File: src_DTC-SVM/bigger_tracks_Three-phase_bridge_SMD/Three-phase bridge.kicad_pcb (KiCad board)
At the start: 2 copper layers, 377.2 x 318 mm, 105 parts, among them M1 MCP6022-I/P, M2 MCP6022-I/P, P1 CONN_1, P2 POWER_FUSE, P3 CONN_2, P4 CONN_1, P5 CONN_1, P6 POWER_FUSE

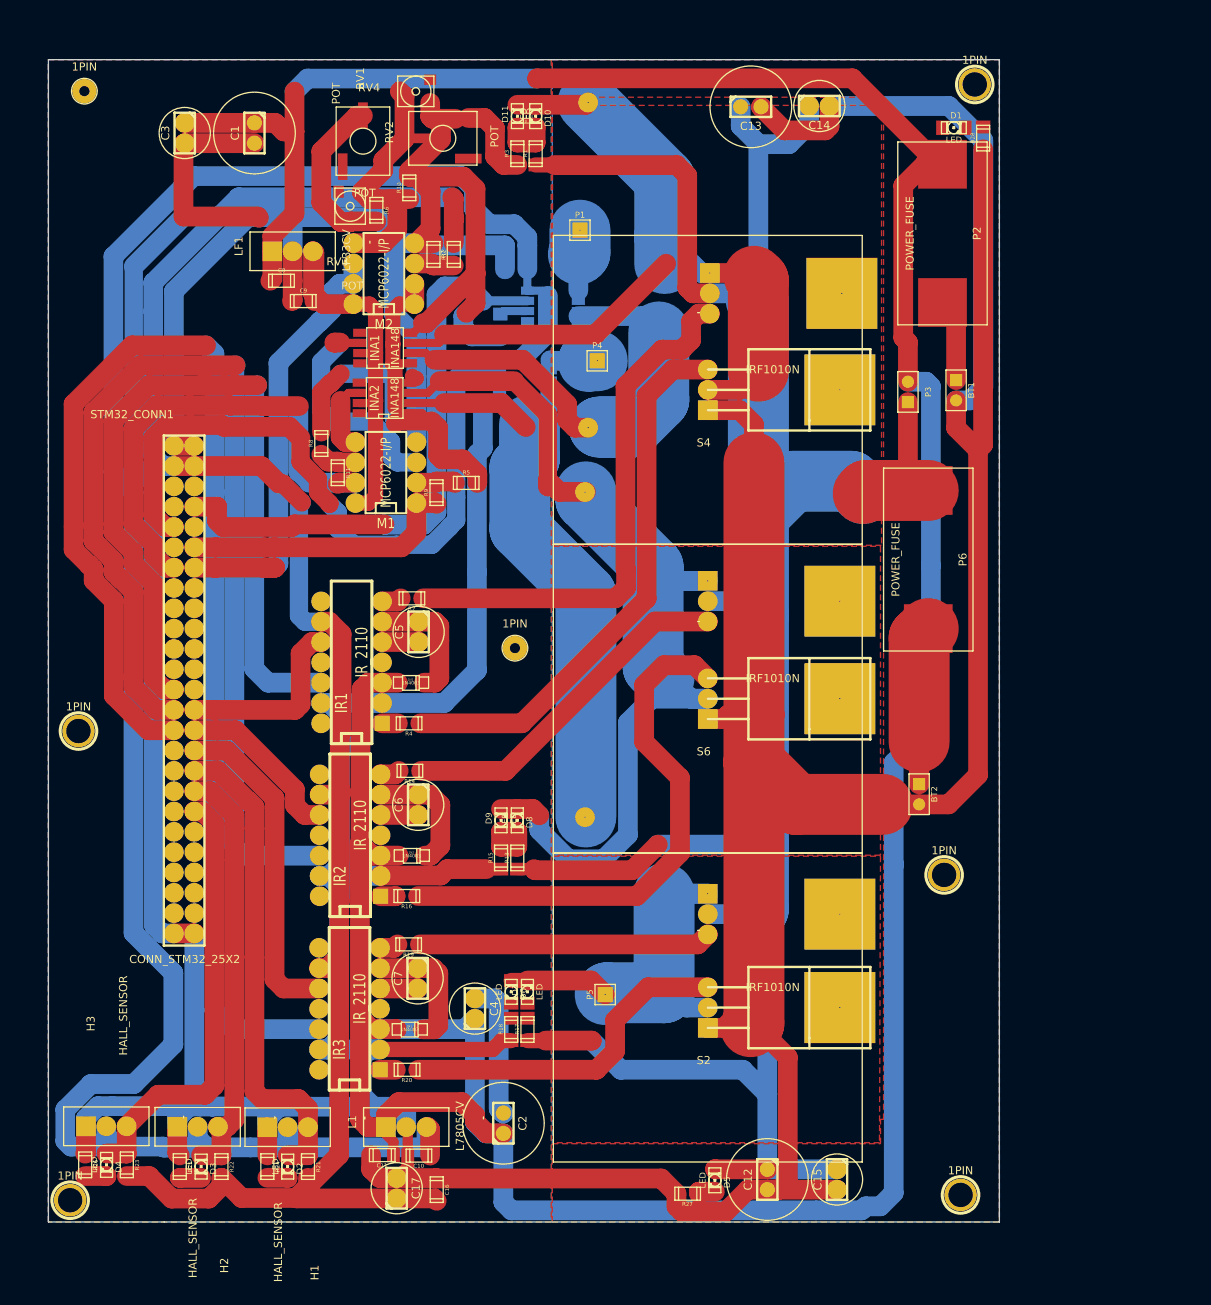
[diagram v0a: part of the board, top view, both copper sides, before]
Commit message: The PCB has been updated with wider tracks and pads (0.097 in, the maximum value before they touch each other).
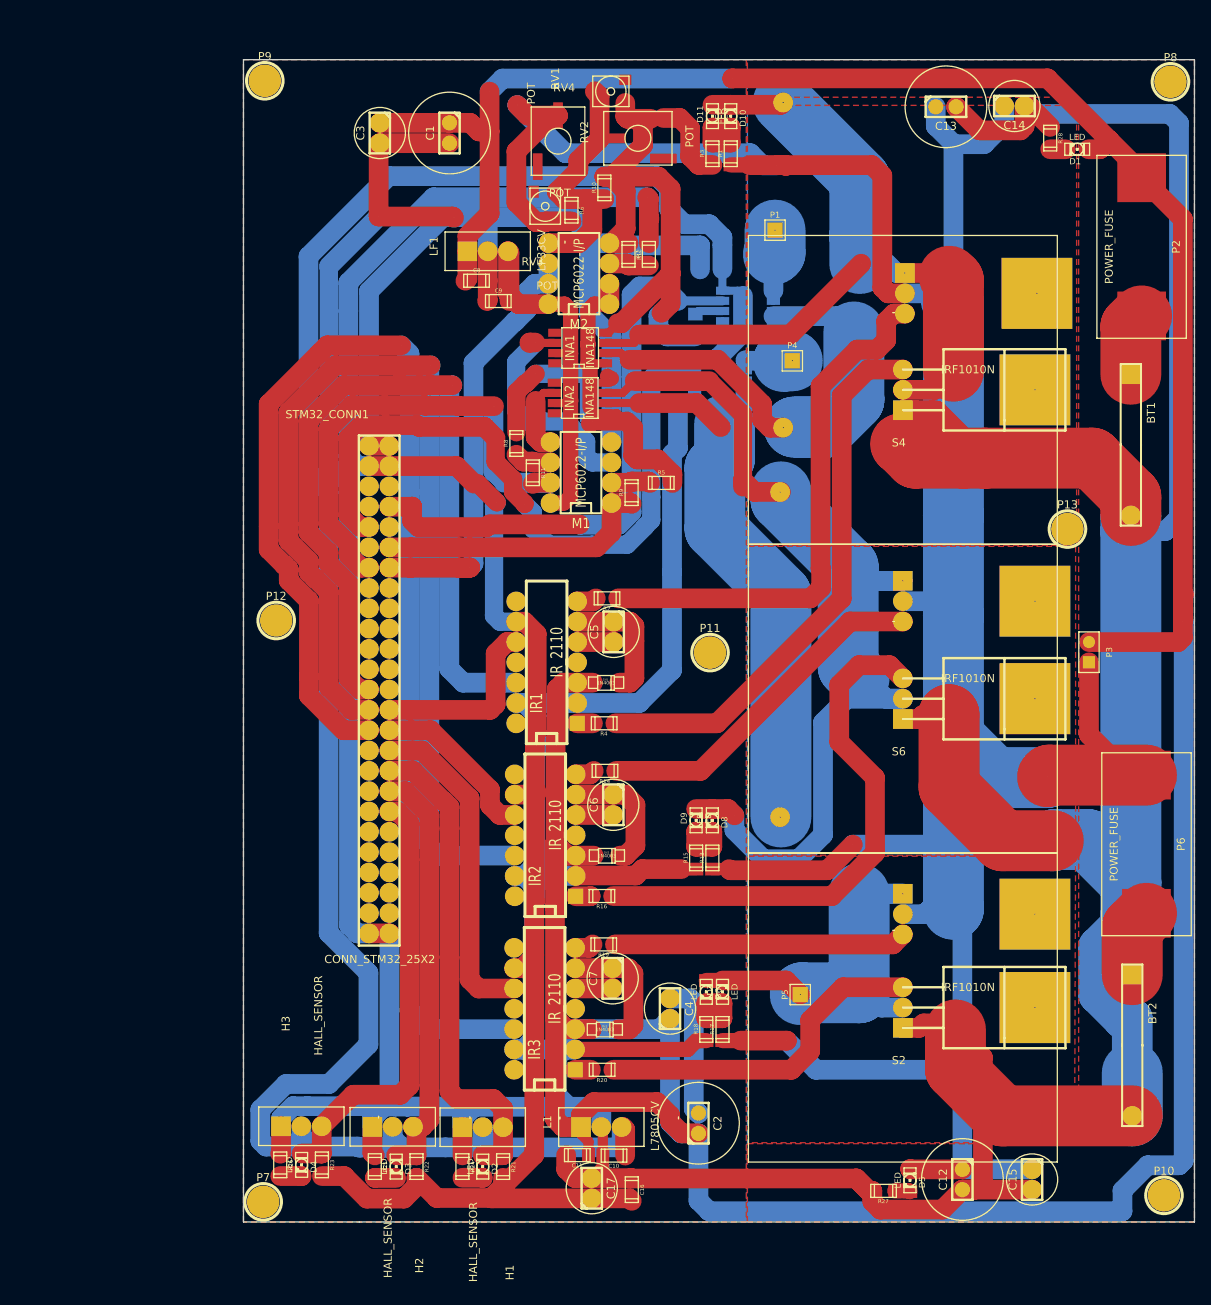
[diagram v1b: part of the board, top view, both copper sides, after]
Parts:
- removed 1PIN (x5): P***, 1pin
- removed 1PIN (x2): P***, 1pin_little
- added P10: CONN_1, 1pin, F.Cu at (272.0, 206.5)
- added P11: CONN_1, 1pin, F.Cu at (215.3, 138.6)
- added P12: CONN_1, 1pin, F.Cu at (161.1, 134.6)
- added P13: CONN_1, 1pin, F.Cu at (260.0, 123.2)
- added P7: CONN_1, 1pin, F.Cu at (159.4, 207.3)
- added P8: CONN_1, 1pin, F.Cu at (272.8, 67.3)
- added P9: CONN_1, 1pin, F.Cu at (159.6, 67.2)
- BT1, BT2: footprint PIN_ARRAY_2X1 -> Battery_2x1
- moved P6 44.8 mm to (269.8, 162.6)
- moved BT2 41.7 mm to (268.1, 188.4)
- moved P3 39.6 mm to (262.7, 138.6)
- moved P2 24.9 mm to (269.2, 87.9)
- moved R27 24.5 mm to (237.0, 205.9)
- moved 1N2 24.4 mm to (202.4, 164.0)
- moved C10 24.4 mm to (203.3, 201.5)
- moved C16 24.4 mm to (205.5, 205.8)
- moved C18 24.4 mm to (215.4, 90.7)
- moved C19 24.4 mm to (213.5, 97.7)
- moved C2 24.4 mm to (213.8, 197.5)
- moved C20 24.4 mm to (215.4, 87.7)
- moved D10 24.4 mm to (217.9, 71.6)
- moved D11 24.4 mm to (215.6, 71.6)
- moved D2 24.4 mm to (186.9, 202.9)
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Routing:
- net +48V: track 338.4 -> 389.8 mm, vias 3 -> 5
- net GND: track 969.6 -> 1007.6 mm, vias 4 -> 5
- net VCC: track 446.7 -> 470.5 mm, vias 2 -> 3
- net N-0000014: track 19.9 -> 8.41 mm
- net N-0000024: track 0.00 -> 7.83 mm
- net N-0000015: track 10.4 -> 7.85 mm
- net N-0000083: track 0.00 -> 1.96 mm
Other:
- board size 377.2 x 318 mm -> 401.6 x 318 mm

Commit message: PCB: Increasing the size of connectors to the motor and eliminating their drill holes. Pending: 	-whether to increase the size of the pads for SMD INA148 and ACS or to change them for through-hole break-out boards.
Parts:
- moved P9 4.33 mm to (162.8, 70.2)
- moved P7 0.62 mm to (159.9, 206.9)
- moved P10 0.61 mm to (271.4, 206.6)
- moved P8 0.58 mm to (272.3, 67.6)
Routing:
- net N-00000112: track 42.7 -> 43.2 mm
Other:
- net class Default: via_dia 0.0254 -> 0.254; via_drill 0.00254 -> 0.127

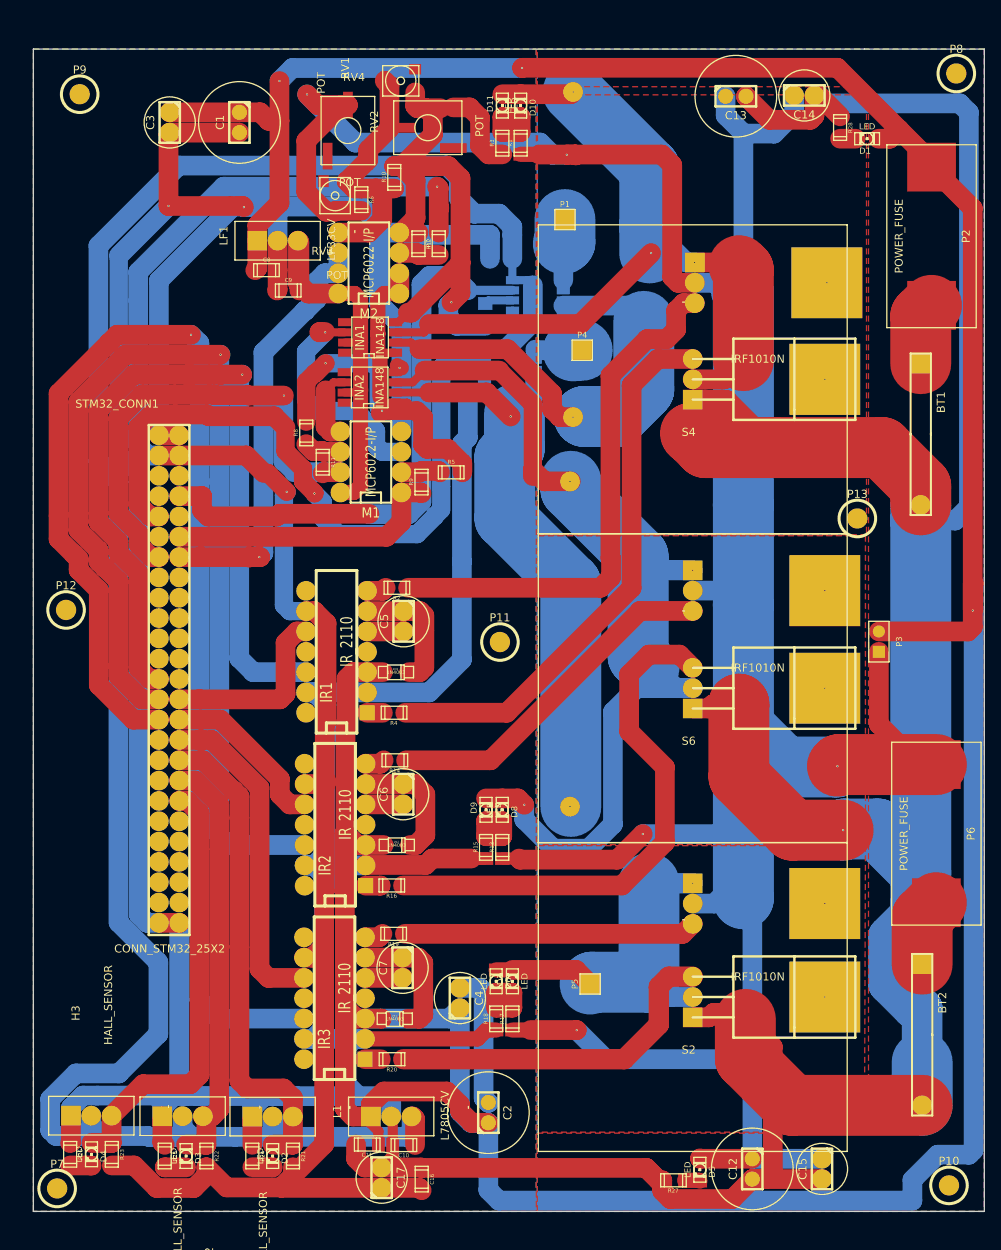
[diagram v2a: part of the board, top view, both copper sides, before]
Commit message: Fixing the pads size error and changing all the pads from rounded to square form.
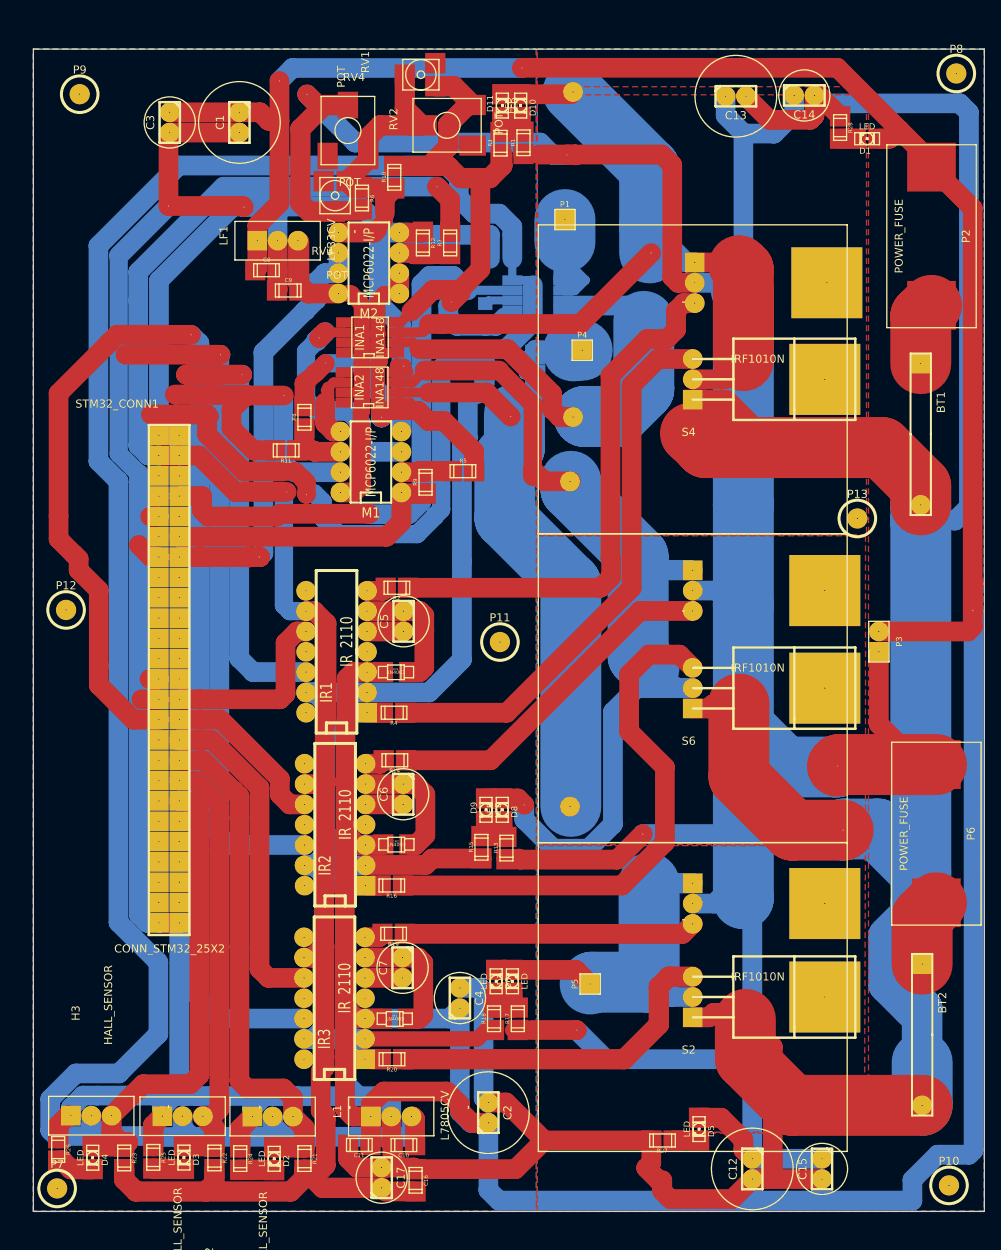
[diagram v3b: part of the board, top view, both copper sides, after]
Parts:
- moved R27 5.16 mm to (235.6, 200.9)
- moved D5 5.08 mm to (240.2, 199.5)
- moved R11 4.80 mm to (188.6, 114.7), turned to 180 degrees
- moved RV1 2.63 mm to (205.4, 67.7)
- moved RV2 2.43 mm to (208.7, 74.0)
- moved R8 1.97 mm to (190.9, 110.5)
- moved R26 1.62 mm to (160.1, 202.1)
- moved R23 1.62 mm to (168.3, 203.1)
- moved R24 1.54 mm to (182.8, 203.2)
- moved R5 1.48 mm to (210.7, 117.3)
- moved R21 1.47 mm to (190.9, 203.2)
- moved R25 1.44 mm to (172.0, 203.0)
- moved R7 1.43 mm to (209.1, 88.7)
- moved R22 1.03 mm to (179.6, 203.1)
- moved C11 0.99 mm to (197.7, 201.5)
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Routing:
- net N-000002: track 103.0 -> 54.0 mm
- net N-000003: track 134.2 -> 85.4 mm
- net GND: track 1007.6 -> 1023.2 mm
- net N-0000038: track 60.3 -> 44.9 mm
- net N-0000082: track 86.5 -> 72.6 mm
- net N-0000084: track 8.92 -> 20.6 mm
- net N-0000097: track 62.2 -> 70.8 mm
- net N-0000021: track 31.7 -> 38.9 mm
- net N-0000018: track 105.2 -> 112.0 mm
- net +48V: track 389.8 -> 395.8 mm
- net N-0000036: track 4.67 -> 8.79 mm
- net +3.3V: track 51.8 -> 55.2 mm
- net N-0000056: track 54.9 -> 58.3 mm
- net N-0000087: track 2.24 -> 4.75 mm
- net N-0000044: track 61.0 -> 63.2 mm
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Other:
- net class Default: via_dia 0.254 -> 0.127; via_drill 0.127 -> 0.1016

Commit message: Updating PCB design.
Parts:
- moved P7 21.5 mm to (161.4, 185.4)
- moved P12 19.1 mm to (161.3, 153.7)
- moved P8 2.16 mm to (270.9, 69.2)
- moved P4 1.06 mm to (224.6, 102.5)
- moved R16 0.72 mm to (202.5, 169.2)
- moved R20 0.64 mm to (202.4, 190.8)
- moved 1N3 0.54 mm to (202.7, 185.7)
- moved 1N2 0.43 mm to (202.8, 164.0)
- moved P10 0.06 mm to (271.4, 206.5)
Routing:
- net N-000002: track 54.0 -> 105.9 mm
- net N-000003: track 85.4 -> 137.0 mm
- net VCC: track 470.2 -> 499.6 mm
- net N-0000038: track 44.9 -> 71.3 mm
- net N-0000082: track 72.6 -> 98.6 mm
- net GND: track 1023.2 -> 1040.4 mm, vias 5 -> 6
- net +48V: track 395.8 -> 408.2 mm, vias 5 -> 6
- net N-000005: track 55.0 -> 63.3 mm
- net N-00000106: track 66.8 -> 61.6 mm
- net N-0000067: track 21.2 -> 25.3 mm
- net +3.3V: track 55.2 -> 59.0 mm
- net N-0000039: track 29.6 -> 32.4 mm
- net N-0000035: track 15.6 -> 18.3 mm
- net N-000007: track 1.98 -> 4.62 mm
- net N-0000017: track 41.2 -> 43.4 mm
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
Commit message: PCB: Fixed missing connection between pins 5 from the IRF2110 to the shunt resistors. The pdf generation for the laser cutter is still pending.
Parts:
- moved P11 58.5 mm to (226.8, 196.0)
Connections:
- C5 pad 2: N-00000108 -> N-0000074
- C6 pad 2: N-0000093 -> N-0000068
- C7 pad 2: N-00000113 -> N-0000076
- D10 pad 1: N-0000018 (its old number) -> N-0000074
- D11 pad 2: N-0000018 (its old number) -> N-0000074
- D6 pad 1: N-000006 (its old number) -> N-0000076
- D7 pad 2: N-000006 (its old number) -> N-0000076
- D8 pad 1: N-0000031 (its old number) -> N-0000068
- D9 pad 2: N-0000031 (its old number) -> N-0000068
- INA1 pad 3: N-0000018 (its old number) -> N-0000074
- INA2 pad 3: N-0000031 (its old number) -> N-0000068
- IR1 pad 5: N-00000108 -> N-0000074
- IR2 pad 5: N-0000093 -> N-0000068
- IR3 pad 5: N-00000113 -> N-0000076
- P5 pad 1: N-000006 (its old number) -> N-0000076
- R_Shunt_1 pad 1: N-0000018 (its old number) -> N-0000074
- R_Shunt_2 pad 1: N-0000031 (its old number) -> N-0000068
- S1 pad 1: N-0000018 (its old number) -> N-0000074
- S2 pad 3: N-000006 (its old number) -> N-0000076
- S3 pad 1: N-0000031 (its old number) -> N-0000068
- S4 pad 3: N-0000018 (its old number) -> N-0000074
- S5 pad 1: N-000006 (its old number) -> N-0000076
- S6 pad 3: N-0000031 (its old number) -> N-0000068
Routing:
- net N-0000068: track 0.00 -> 273.7 mm, vias 0 -> 1
- net N-0000074: track 0.00 -> 201.6 mm, vias 0 -> 2
- net N-0000031 (its old number): track 146.4 -> 0.00 mm, vias 1 -> 0
- net N-0000018 (its old number): track 112.0 -> 0.00 mm, vias 1 -> 0
- net N-0000076: track 0.00 -> 79.6 mm
- net N-000006 (its old number): track 45.4 -> 0.00 mm
- net GND: track 1040.4 -> 1061.5 mm
- net N-00000113: track 4.77 -> 0.00 mm
- net N-0000093: track 4.70 -> 0.00 mm
- net N-00000108: track 4.64 -> 0.00 mm
- net N-00000107: track 68.9 -> 65.2 mm
- added copper zone on F.Cu, net N-0000068
- added copper zone on F.Cu, net N-0000074
- added copper zone on F.Cu, net N-0000076
- removed copper zone on F.Cu, net N-0000018 (its old number)
- removed copper zone on F.Cu, net N-0000031 (its old number)
- removed copper zone on F.Cu, net N-000006 (its old number)
